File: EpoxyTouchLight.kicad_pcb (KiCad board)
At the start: 2 copper layers, 66 x 66 mm, 22 parts, among them J1 Serial, SW1 SW_DPDT_x2, SW2 Button, U1 ESP32-WROOM-32

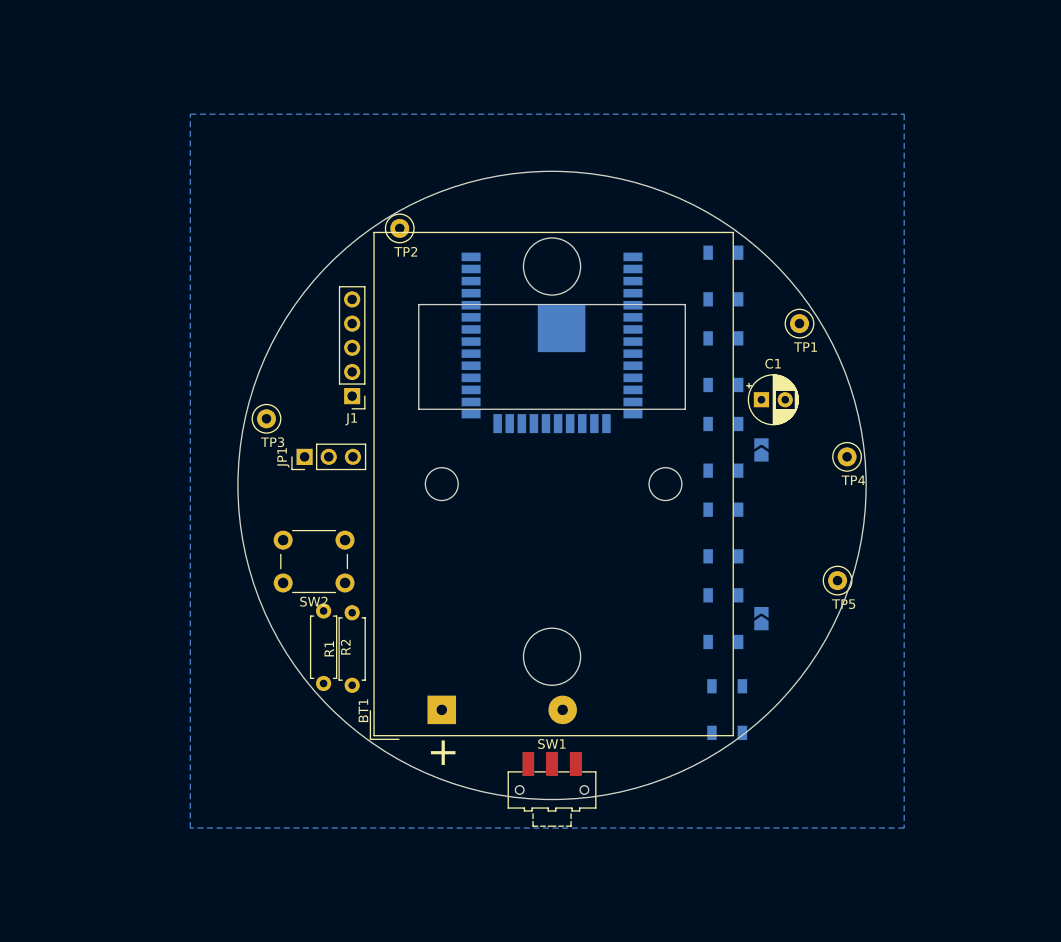
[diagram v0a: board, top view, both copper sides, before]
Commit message: Add radio receiver module
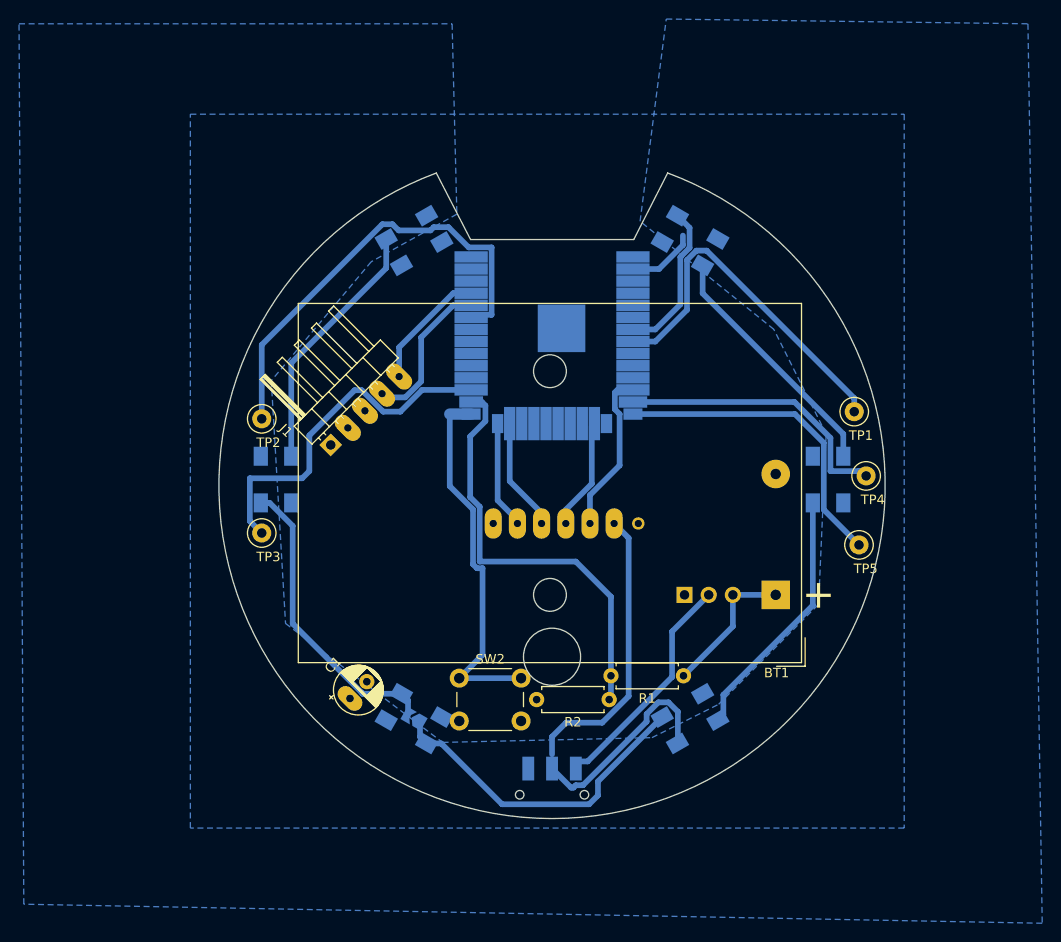
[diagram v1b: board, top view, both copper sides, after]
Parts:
- removed JP2: Skip, Jumper:SolderJumper-2_P1.3mm_Open_TrianglePad1.0x1.5mm
- added U2: radio-receiver, radio-receiver:radio-receiver, B.Cu at (109.1, 104.0)
- J1: footprint Connector_PinHeader_2.54mm:PinHeader_1x05_P2.54mm_Vertical -> Connector_PinHeader_2.54mm:PinHeader_1x05_P2.54mm_Horizontal; moved to B.Cu
- JP1: footprint Connector_PinHeader_2.54mm:PinHeader_1x03_P2.54mm_Vertical -> Connector_PinHeader_2.54mm:PinHeader_1x03_P2.54mm_Horizontal; moved to B.Cu
- SW1: moved to B.Cu
- moved C1 53.4 mm to (78.8, 122.4), turned to 45 degrees
- moved D5 47.3 mm to (71.0, 99.4)
- moved JP3 46.1 mm to (85.5, 124.5), turned to 150 degrees
- moved JP1 42.5 mm to (113.9, 111.5), turned to -90 degrees
- moved D6 39.1 mm to (85.5, 74.3), turned to -150 degrees
- moved BT1 37.1 mm to (123.5, 111.5), turned to 180 degrees
- moved R1 34.8 mm to (113.8, 120.0), turned to 180 degrees
- moved D4 34.2 mm to (85.5, 124.5), turned to -30 degrees
- moved R2 31.4 mm to (106.0, 122.5), turned to 180 degrees
- moved TP2 24.7 mm to (69.5, 93.0)
- moved D2 24.0 mm to (129.0, 99.4), turned to 90 degrees
- moved SW2 15.6 mm to (90.2, 120.2), turned to 0 degrees
- moved D1 13.2 mm to (114.5, 74.3), turned to 150 degrees
- moved TP3 12.0 mm to (69.5, 105.0)
- moved TP1 10.9 mm to (131.8, 92.2)
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- renumbered D5 to D1, D6 to D2, D1 to D3, D2 to D4, D3 to D5, D4 to D6
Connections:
- D1 pad 4: Net-(D4-Pad2) -> Neopixel
- D2 pad 2: unconnected-(D6-Pad2) -> Net-(D2-Pad2)
- D3 pad 2: Net-(D1-Pad2) (its old number) -> Net-(D3-Pad2)
- D3 pad 4: Neopixel -> Net-(D2-Pad2)
- D4 pad 2: Net-(D2-Pad2) -> Net-(D4-Pad2)
- D4 pad 4: Net-(D1-Pad2) (its old number) -> Net-(D3-Pad2)
- D5 pad 2: Net-(D3-Pad2) -> Net-(D5-Pad2)
- D5 pad 4: Net-(D2-Pad2) -> Net-(D4-Pad2)
- D6 pad 2: Net-(D4-Pad2) -> unconnected-(D6-Pad2)
- D6 pad 4: Net-(D3-Pad2) -> Net-(D5-Pad2)
- U1 pad 12: unconnected-(U1-Pad12) -> RADIO-0
- U1 pad 16: unconnected-(U1-Pad16) -> RADIO-1
- U1 pad 23: unconnected-(U1-Pad23) -> RADIO-2
- U1 pad 24: unconnected-(U1-Pad24) -> RADIO-3
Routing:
- net +3V3: track 0.00 -> 59.7 mm
- net TOUCH-8: track 0.00 -> 48.0 mm
- net BATTERY_METER: track 0.00 -> 45.3 mm
- net FLASH: track 0.00 -> 39.3 mm
- net TOUCH-9: track 0.00 -> 38.1 mm
- net TOUCH-7: track 0.00 -> 37.4 mm
- net Net-(D3-Pad2): track 0.00 -> 34.6 mm
- net TOUCH-5: track 0.00 -> 33.6 mm
- net Net-(D4-Pad2): track 0.00 -> 31.8 mm
- net TOUCH-6: track 0.00 -> 30.1 mm
- net Net-(D5-Pad2): track 0.00 -> 27.0 mm
- net Net-(D2-Pad2): track 0.00 -> 27.0 mm
- net Net-(D1-Pad2): track 0.00 -> 26.3 mm
- net Net-(JP1-Pad2): track 0.00 -> 24.0 mm
- net RADIO-0: track 0.00 -> 17.3 mm
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- added copper zone on B.Cu, net +3V3
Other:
- board size 66 x 66 mm -> 70 x 67.8 mm
